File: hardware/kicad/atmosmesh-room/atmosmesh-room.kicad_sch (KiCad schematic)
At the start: 26 parts, among them U1 IDEASPARK_ESP32_1V14_TFT_30PIN

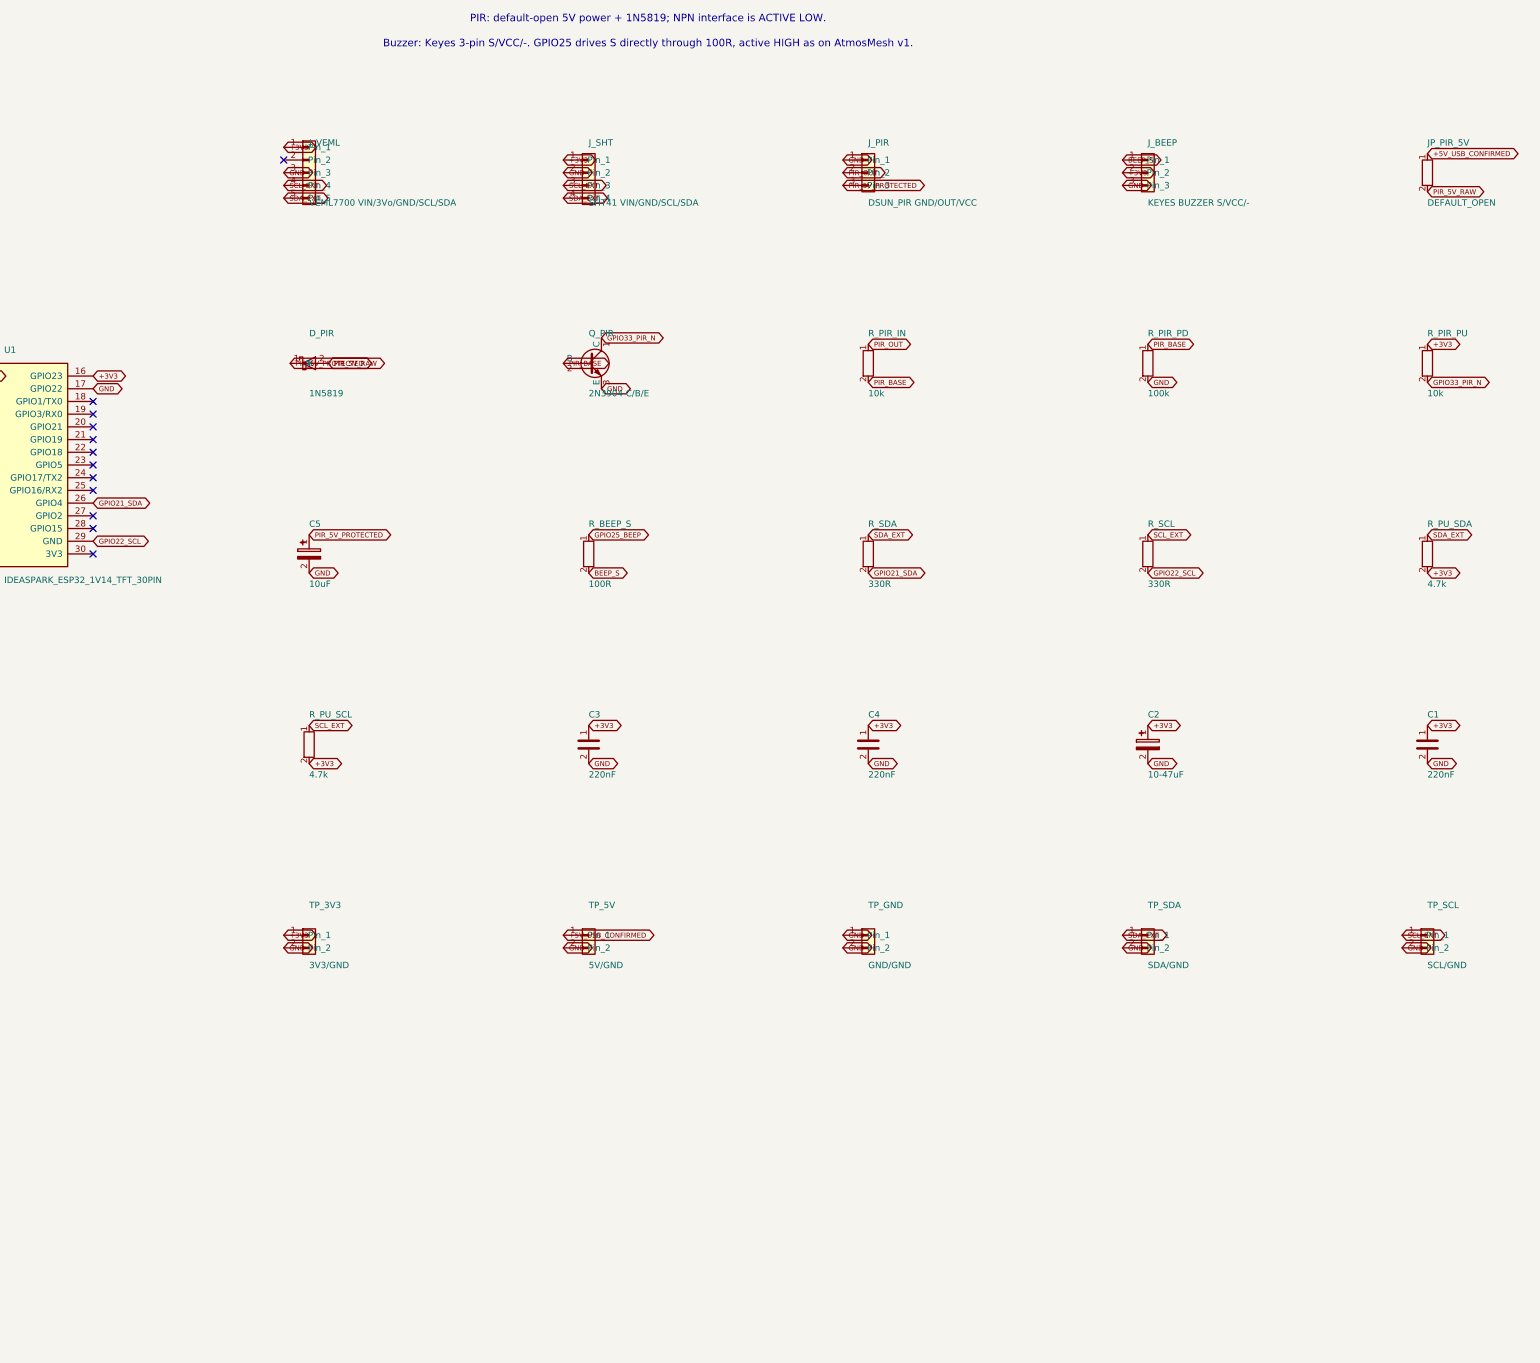
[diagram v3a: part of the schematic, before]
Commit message: :sparkles: feat(room): add the SDS011 with the protection the bench fault earned
ROOM-02. The operator asked for the SDS011 that already worked on AtmosMesh v1,
with additional protection. The protection is aimed at a specific, recorded
failure rather than at hazards in general.

On 2026-08-17 this sensor was wired straight through: its push-pull TXD landed
on the ESP32's push-pull TX2 and the two fought on one net for roughly 10 ms in
every second, against a 40 mA absolute maximum. So:

- The UART is crossed. Sensor TXD reaches GPIO16/RX2, GPIO17/TX2 reaches sensor
  RXD, each through 1k. That bounds a driver fight to about 3.3 mA. At 9600 baud
  a bit is 104 us while 1k into a few hundred pF settles in a couple of hundred
  nanoseconds, so it costs nothing in signal terms.
- generate_project.py refuses to emit a straight-through SDS011 UART.

The PIR's 1N5819 idiom deliberately does NOT transfer to this rail. The SDS011
minimum is 4.7 V and a Schottky drops 0.3-0.4 V at fan current, landing under
the minimum before any USB droop is counted. JP_SDS_5V is default-open instead,
isolating at zero volts, and the generator refuses a diode on that rail.

Both guards are mutation-proved: swapping the header's RXD/TXD nets raises, and
adding a Schottky to the rail raises.

Three power facts are assumed and gate closing the jumper, recorded in D-026 and
as unchecked ROOM-02 criteria rather than left silent: VIN may already sit near
4.6-4.7 V behind a VBUS diode, the shared rail is already near 650 mA peak
coincidence without this sensor, and C6 at 10 uF is not shown to meet the
<20 mV ripple specification against a fan.

Gates: ERC 0, DRC 0 violations and 0 parity problems, structural validation
PASS, git diff --check clean.
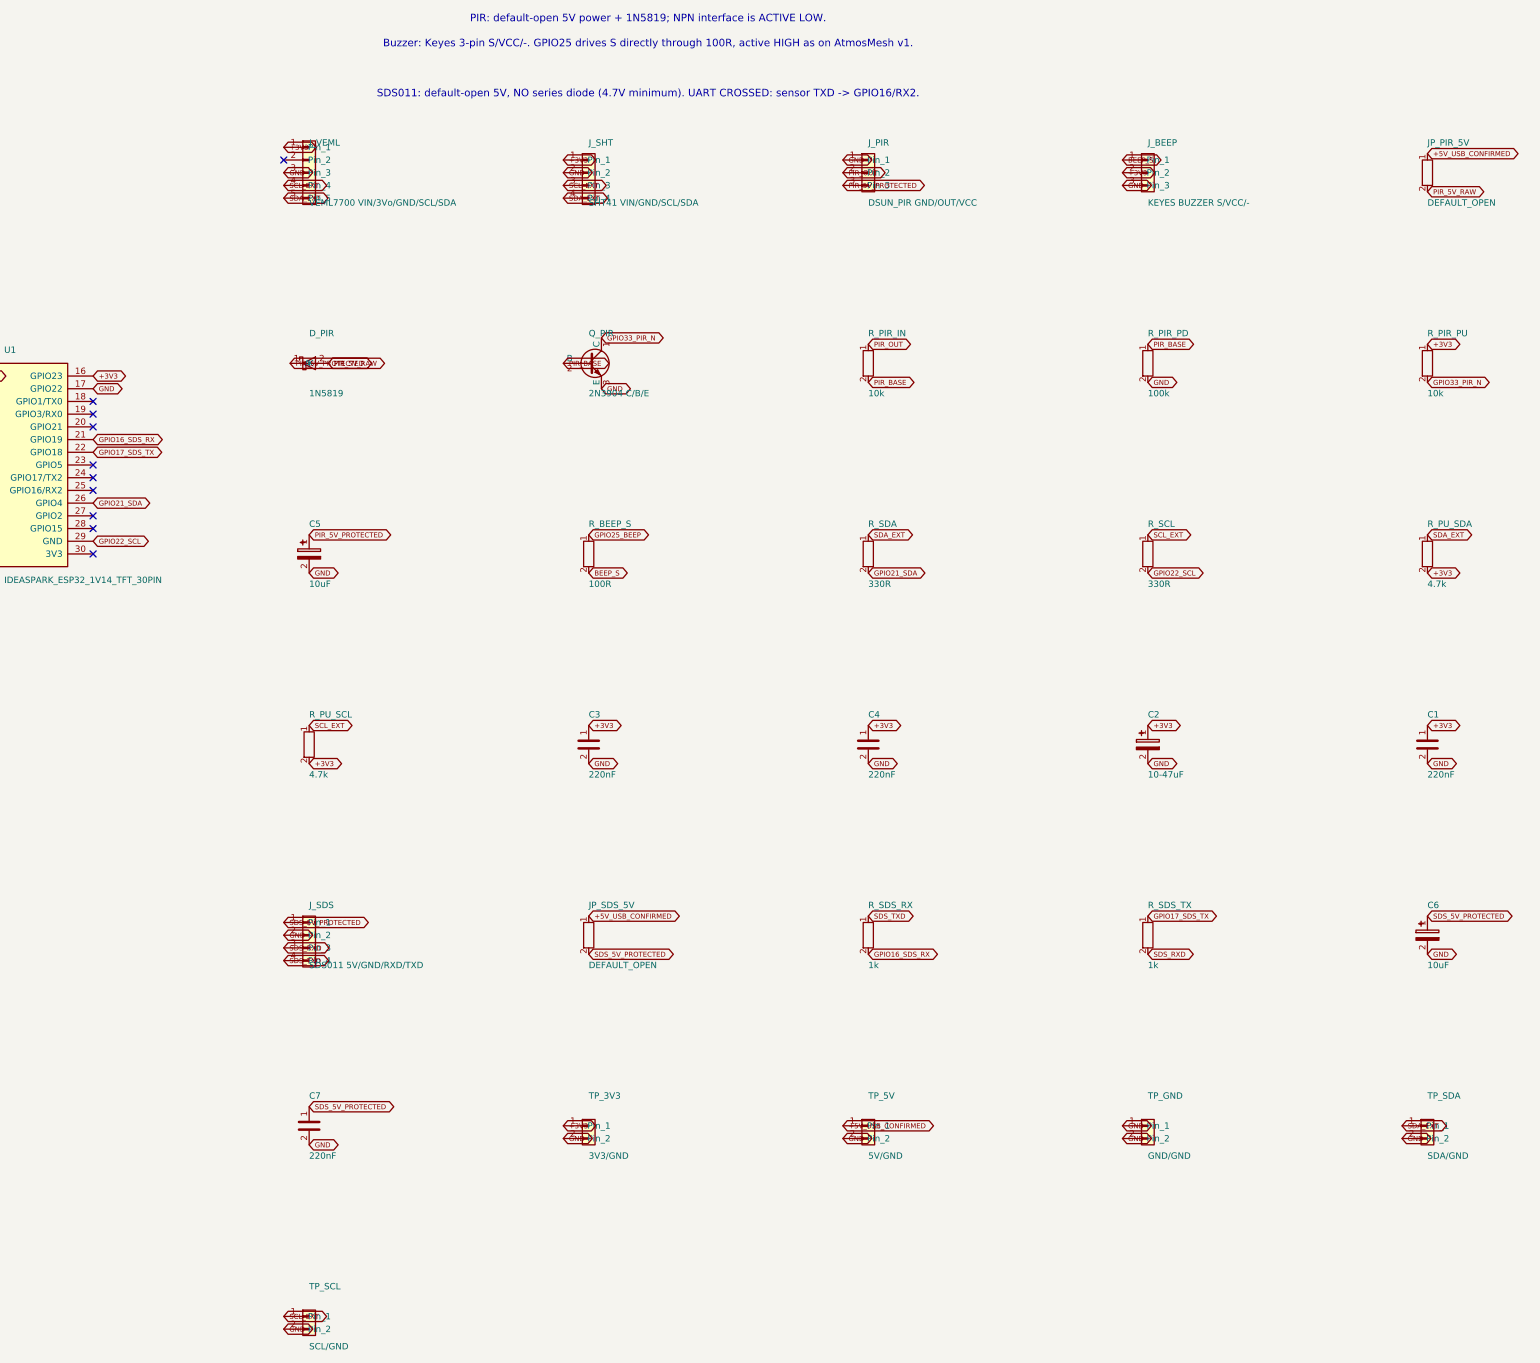
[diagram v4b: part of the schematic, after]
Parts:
- added C6: 10uF, room:C_Radial_P2.00mm, symbol atmosmesh:C_Polarized
- added C7: 220nF, room:C_Disc_P5.00mm, symbol atmosmesh:C
- added JP_SDS_5V: DEFAULT_OPEN, room:Jumper_2_Open_P2.54mm, symbol atmosmesh:R
- added J_SDS: SDS011 5V/GND/RXD/TXD, room:PinHeader_1x04_P2.54mm, symbol atmosmesh:Conn_01x04
- added R_SDS_RX, R_SDS_TX: 1k, room:R_Axial_P7.62mm, symbol atmosmesh:R
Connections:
- net +5V_USB_CONFIRMED: now also JP_SDS_5V.1
- net GND: now also C6.2, C7.2, J_SDS.2 (Pin_2)
- net GPIO16_SDS_RX: now reaches U1.21 (GPIO19)
- net GPIO16_SDS_RX: now also R_SDS_RX.2
- net GPIO17_SDS_TX: now reaches U1.22 (GPIO18)
- net GPIO17_SDS_TX: now also R_SDS_TX.1
- new net SDS_5V_PROTECTED: C6.1, C7.1, JP_SDS_5V.2, J_SDS.1 (Pin_1)
- new net SDS_RXD: J_SDS.3 (Pin_3), R_SDS_TX.2
- new net SDS_TXD: J_SDS.4 (Pin_4), R_SDS_RX.1
- no-connect marks 23 -> 21
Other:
- note added: "SDS011: default-open 5V, NO series diode (4.7V minimum). UART CROSSED: sensor TXD -> GPIO16/RX2."
- moved on the sheet: TP_3V3, TP_5V, TP_GND, TP_SCL, TP_SDA
